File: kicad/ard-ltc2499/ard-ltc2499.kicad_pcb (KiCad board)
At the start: 2 copper layers, 68.6 x 53.3 mm, 8 parts, among them P1 Power, P2 Analog, P3 Digital, P4 Digital, P5 CONN_01X01, P6 CONN_01X01, P7 CONN_01X01, P8 CONN_01X01

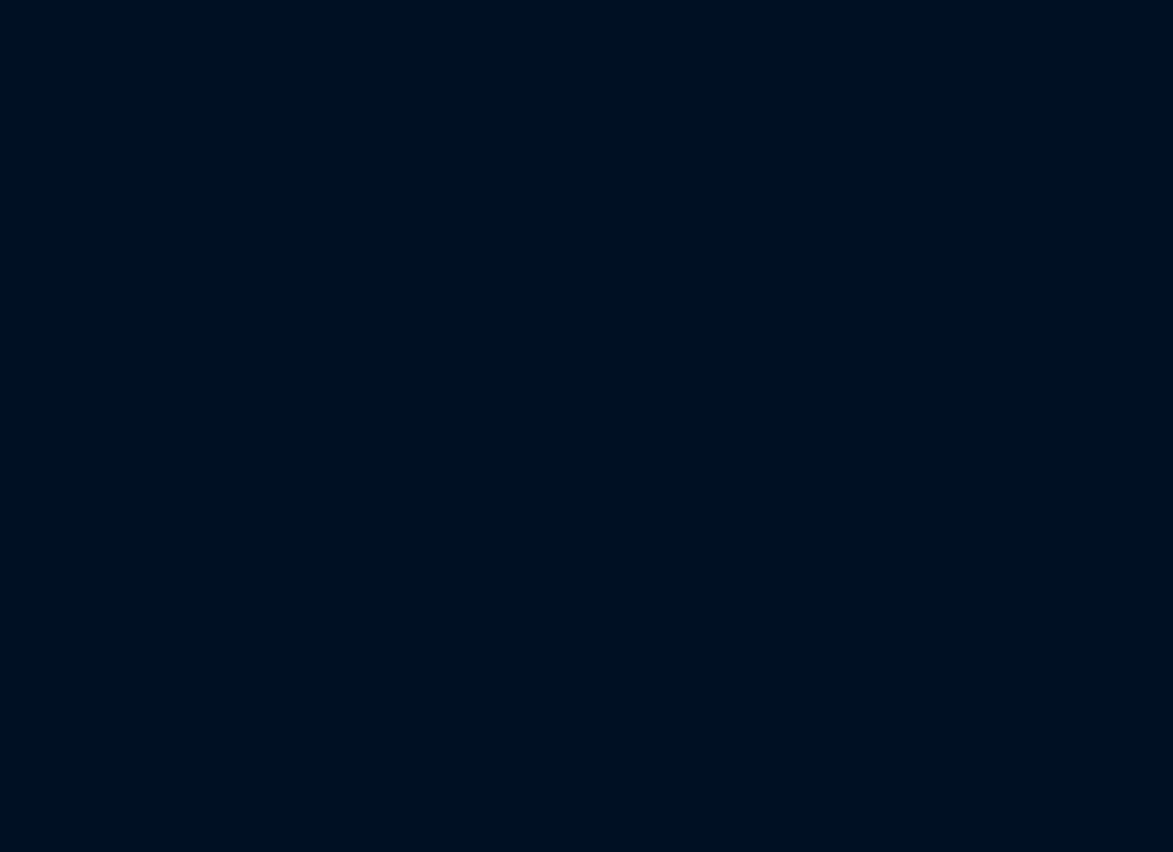
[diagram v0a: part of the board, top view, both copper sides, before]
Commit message: Updated PCB with schematic edits
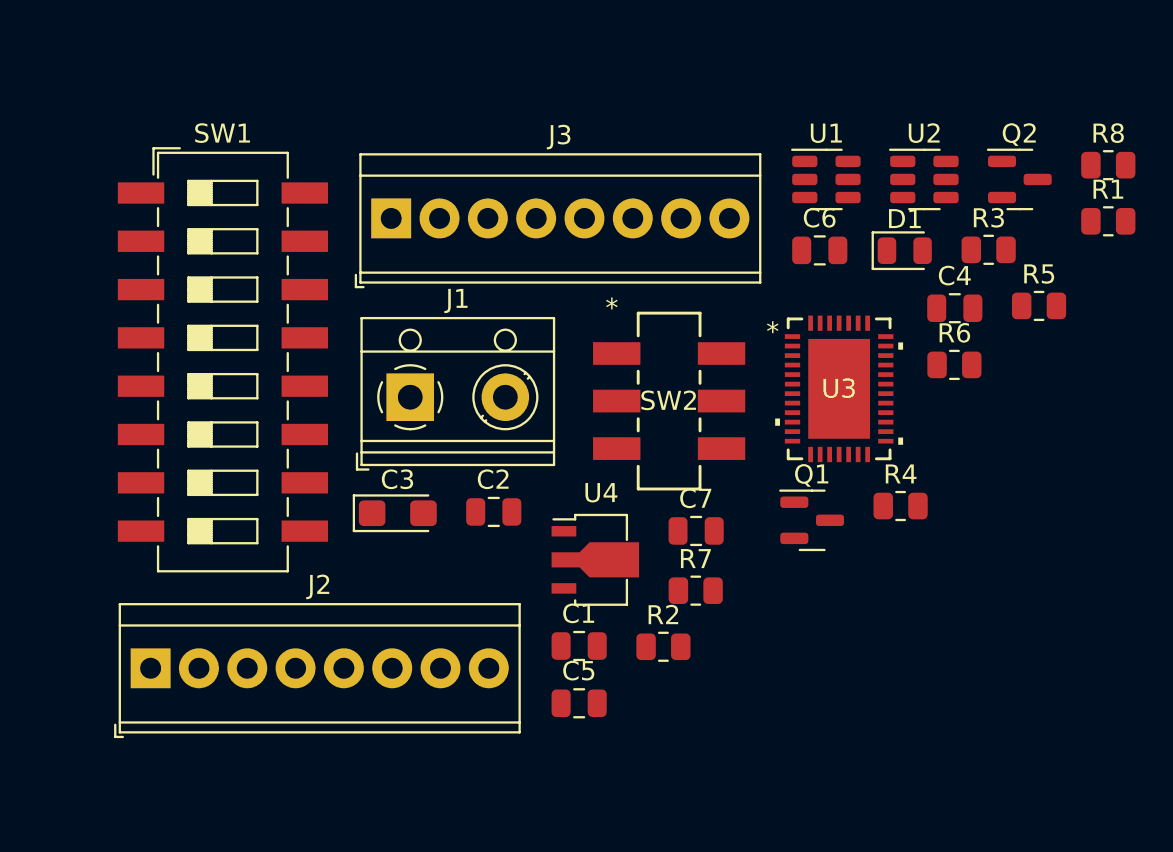
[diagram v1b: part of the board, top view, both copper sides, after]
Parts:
- added C1: 0.1uF, Capacitor_SMD:C_0805_2012Metric, F.Cu at (213.7, 111.5)
- added C2: 1uF, Capacitor_SMD:C_0805_2012Metric, F.Cu at (209.2, 104.4)
- added C3: 22uF, Capacitor_Tantalum_SMD:CP_EIA-3216-18_Kemet-A, F.Cu at (204.1, 104.5)
- added C4: 0.1uF, Capacitor_SMD:C_0805_2012Metric, F.Cu at (233.4, 93.7)
- added C5: 10uF, Capacitor_SMD:C_0805_2012Metric, F.Cu at (213.7, 114.5)
- added C6: 10uF, Capacitor_SMD:C_0805_2012Metric, F.Cu at (226.3, 90.7)
- added C7: 2.2uF, Capacitor_SMD:C_0805_2012Metric, F.Cu at (219.8, 105.4)
- added D1: GREEN LED, LED_SMD:LED_0805_2012Metric, F.Cu at (230.8, 90.7)
- added J1: Screw_Terminal_01x02, TerminalBlock_RND:TerminalBlock_RND_205-00012_1x02_P5.00mm_Horizontal, F.Cu at (204.8, 98.4)
- added J2: Screw_Terminal_01x08, TerminalBlock_TE-Connectivity:TerminalBlock_TE_282834-8_1x08_P2.54mm_Horizontal, F.Cu at (191.1, 112.7)
- added J3: Screw_Terminal_01x08, TerminalBlock_TE-Connectivity:TerminalBlock_TE_282834-8_1x08_P2.54mm_Horizontal, F.Cu at (203.8, 89.0)
- added Q1: BSS138, Package_TO_SOT_SMD:SOT-23, F.Cu at (225.9, 104.9)
- added Q2: BSS138, Package_TO_SOT_SMD:SOT-23, F.Cu at (236.8, 87.0)
- added R1: 10k, Resistor_SMD:R_0805_2012Metric, F.Cu at (241.5, 89.2)
- added R2: 10k, Resistor_SMD:R_0805_2012Metric, F.Cu at (218.1, 111.5)
- added R3: 1k, Resistor_SMD:R_0805_2012Metric, F.Cu at (235.2, 90.7)
- added R4: 10k, Resistor_SMD:R_0805_2012Metric, F.Cu at (230.6, 104.1)
- added R5: 10k, Resistor_SMD:R_0805_2012Metric, F.Cu at (237.8, 93.6)
- added R6: 10k, Resistor_SMD:R_0805_2012Metric, F.Cu at (233.4, 96.7)
- added R7: 10k, Resistor_SMD:R_0805_2012Metric, F.Cu at (219.8, 108.6)
- added R8: 1k, Resistor_SMD:R_0805_2012Metric, F.Cu at (241.5, 86.2)
- added SW1: SW_DIP_x08, Button_Switch_SMD:SW_DIP_SPSTx08_Slide_6.7x21.88mm_W8.61mm_P2.54mm_LowProfile, F.Cu at (194.9, 96.6)
- added SW2: SW_Push_DPDT, ISE_UltraLibrarian:SW_JS202011SCQN, F.Cu at (218.4, 98.6)
- added U1: LT6654xxS6, Package_TO_SOT_SMD:TSOT-23-6, F.Cu at (226.7, 87.0)
- added U2: 24AA025E64, Package_TO_SOT_SMD:TSOT-23-6, F.Cu at (231.8, 87.0)
- added U3: LTC2499CUHF-PBF, ISE_UltraLibrarian:QFN-38_UHF_LIT, F.Cu at (227.3, 98.0)
- added U4: AP7381-50Y, ISE_Generic:SOT-89-3, F.Cu at (214.5, 107.0)
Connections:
- net /10(**/SS) renamed /10(**/SS)
- net /11(**/MOSI) renamed /11(**/MOSI)
- P1 pad 1: Net-(P1-Pad1) -> unconnected-(P1-Pad1)
- P2 pad 5: /A4(SDA) -> /A4
- P2 pad 6: /A5(SCL) -> /A5
- P3 pad 1: /A5(SCL) -> /SCL
- P3 pad 2: /A4(SDA) -> /SDA
- P5 pad 1: Net-(P5-Pad1) -> unconnected-(P5-Pad1)
- P6 pad 1: Net-(P6-Pad1) -> unconnected-(P6-Pad1)
- P7 pad 1: Net-(P7-Pad1) -> unconnected-(P7-Pad1)
- P8 pad 1: Net-(P8-Pad1) -> unconnected-(P8-Pad1)

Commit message: Initial placement
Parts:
- added R10: 1k, Resistor_SMD:R_0805_2012Metric, F.Cu at (195.2, 119.5)
- added R9: 1k, Resistor_SMD:R_0805_2012Metric, F.Cu at (195.2, 122.5)
- added TP1: TestPoint, TestPoint:TestPoint_Pad_D1.5mm, B.Cu at (150.2, 60.8)
- added TP10: TestPoint, TestPoint:TestPoint_Pad_D1.5mm, B.Cu at (132.1, 66.9)
- added TP11: TestPoint, TestPoint:TestPoint_Pad_D1.5mm, B.Cu at (142.5, 130.8)
- added TP12: TestPoint, TestPoint:TestPoint_Pad_D1.5mm, F.Cu at (112.1, 104.5)
- added TP13: TestPoint, TestPoint:TestPoint_Pad_D1.5mm, B.Cu at (134.6, 66.0)
- added TP14: TestPoint, TestPoint:TestPoint_Pad_D1.5mm, B.Cu at (145.0, 129.9)
- added TP15: TestPoint, TestPoint:TestPoint_Pad_D1.5mm, B.Cu at (137.2, 66.9)
- added TP16: TestPoint, TestPoint:TestPoint_Pad_D1.5mm, B.Cu at (147.6, 130.8)
- added TP17: TestPoint, TestPoint:TestPoint_Pad_D1.5mm, B.Cu at (139.7, 66.0)
- added TP18: TestPoint, TestPoint:TestPoint_Pad_D1.5mm, B.Cu at (150.1, 129.9)
- added TP2: TestPoint, TestPoint:TestPoint_Pad_D1.5mm, B.Cu at (121.9, 66.9)
- added TP3: TestPoint, TestPoint:TestPoint_Pad_D1.5mm, B.Cu at (132.3, 130.8)
- added TP4: TestPoint, TestPoint:TestPoint_Pad_D1.5mm, B.Cu at (124.5, 66.0)
- added TP5: TestPoint, TestPoint:TestPoint_Pad_D1.5mm, B.Cu at (134.9, 129.9)
- added TP6: TestPoint, TestPoint:TestPoint_Pad_D1.5mm, B.Cu at (127.0, 66.9)
- added TP7: TestPoint, TestPoint:TestPoint_Pad_D1.5mm, B.Cu at (137.4, 130.8)
- added TP8: TestPoint, TestPoint:TestPoint_Pad_D1.5mm, B.Cu at (129.5, 66.0)
- added TP9: TestPoint, TestPoint:TestPoint_Pad_D1.5mm, B.Cu at (140.0, 129.9)
- SW2: value SW_Push_DPDT -> JS202011SCQN
- moved C6 99.4 mm to (128.5, 108.6), turned to 90 degrees
- moved R8 88.9 mm to (161.3, 124.5)
- moved C7 86.5 mm to (133.3, 106.8), turned to 180 degrees
- moved C5 85.8 mm to (128.5, 103.5), turned to -90 degrees
- moved SW2 84.9 mm to (133.5, 97.8), turned to 90 degrees
- moved C4 83.4 mm to (150.4, 101.3)
- moved U1 82.5 mm to (145.0, 92.1), turned to -90 degrees
- moved U3 82.0 mm to (132.6, 111.4), turned to -90 degrees
- moved D1 81.5 mm to (156.6, 124.5)
- moved R1 81.1 mm to (160.7, 95.9)
- moved J3 80.9 mm to (132.3, 126.9)
- moved R5 79.4 mm to (160.2, 77.4)
- moved R6 79.4 mm to (155.7, 80.5)
- moved U2 78.3 mm to (150.4, 104.6), turned to 180 degrees
- moved R4 73.0 mm to (161.2, 81.4)
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- renumbered U3 to U1, U1 to U2, U4 to U3, U2 to U4
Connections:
- SW1 pad 4: Net-(R3-Pad1) -> Net-(R10-Pad1)
- SW1 pad 6: Net-(R3-Pad1) -> Net-(R9-Pad1)
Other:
- board size 68.6 x 53.3 mm -> 53.3 x 68.6 mm
- board text added: "*"
- board text added: "0 1 2 3 4 5 6 7"
- board text added: "10 11 12 13 14 15"
- board text added: "8 9"
- board text added: "A0 A1 A2 A3 A4 A5"
- board text added: "D7 D6 D5 D4 D3 D2 TX/D1 RX/D0"
- board text added: "N/C IOREF RST 3.3V 5V GND GND VIN"
- board text added: "SCL SDA AREF GND D13 D12 D11 D10 D9 D8"
- board text removed: "1"

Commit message: Complete PCB
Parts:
- TP12: moved to B.Cu
- moved R3 44.8 mm to (163.4, 95.5)
- moved R9 43.5 mm to (163.4, 92.7)
- moved R10 43.4 mm to (163.4, 89.9)
- moved SW1 32.0 mm to (160.1, 112.0)
- moved R8 29.8 mm to (132.6, 116.6)
- moved TP12 24.9 mm to (136.4, 109.7), turned to 180 degrees
- moved D1 24.5 mm to (132.6, 119.4), turned to 180 degrees
- moved R7 17.0 mm to (165.9, 69.1), turned to 90 degrees
- moved C1 13.9 mm to (163.6, 78.0)
- moved R1 13.9 mm to (160.0, 82.0)
- moved R2 13.9 mm to (160.0, 84.8)
- moved U4 13.9 mm to (160.0, 78.0)
- moved R4 12.2 mm to (169.7, 72.6), turned to 180 degrees
- moved R6 11.6 mm to (157.6, 69.1), turned to 90 degrees
- moved Q1 8.85 mm to (169.7, 69.1)
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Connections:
- P3 pad 4: GND -> unconnected-(P3-Pad4)
- R1 pad 1: /A0 -> /AD0
- R2 pad 1: /A1 -> /AD1
- SW1 pad 1: GND -> /CA2
- SW1 pad 10: /CA0 -> GND
- SW1 pad 11: /CA1 -> GND
- SW1 pad 12: /CA1 -> Net-(R10-Pad1)
- SW1 pad 13: /CA2 -> GND
- SW1 pad 14: /CA2 -> Net-(R9-Pad1)
- SW1 pad 15: /A0 -> GND
- SW1 pad 16: /A1 -> Net-(R3-Pad1)
- SW1 pad 2: GND -> /CA2
- SW1 pad 3: GND -> /CA1
- SW1 pad 4: Net-(R10-Pad1) -> /CA1
- SW1 pad 5: GND -> /CA0
- SW1 pad 6: Net-(R9-Pad1) -> /CA0
- SW1 pad 7: GND -> /AD1
- SW1 pad 8: Net-(R3-Pad1) -> /AD0
- SW1 pad 9: /CA0 -> GND
- U4 pad 4: /A1 -> /AD1
- U4 pad 5: /A0 -> /AD0
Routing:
- net GND: track 0.00 -> 112.0 mm, vias 0 -> 22
- net VCC: track 0.00 -> 104.2 mm, vias 0 -> 27
- net /IOREF: track 0.00 -> 80.4 mm
- net /AD0: track 0.00 -> 46.1 mm
- net /VREF: track 0.00 -> 44.1 mm, vias 0 -> 3
- net Net-(J3-Pad1): track 0.00 -> 43.1 mm
- net /AD1: track 0.00 -> 42.7 mm
- net Net-(J3-Pad2): track 0.00 -> 40.5 mm
- net Net-(J3-Pad3): track 0.00 -> 39.7 mm
- net Net-(J3-Pad7): track 0.00 -> 38.5 mm
- net Net-(J3-Pad8): track 0.00 -> 38.4 mm
- net Net-(J3-Pad4): track 0.00 -> 37.5 mm
- net /SCL_5V: track 0.00 -> 37.4 mm
- net Net-(J3-Pad5): track 0.00 -> 36.8 mm
- net Net-(J3-Pad6): track 0.00 -> 36.7 mm
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- added copper zone on F.Cu, net /VREF
- added copper zone on F.Cu, net /Vin
- added copper zone on B.Cu, net GND
- added copper zone on F.Cu, net GND
- added copper zone on B.Cu, net VCC
- added copper zone on F.Cu, net VCC
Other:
- board text added: "4.096V REF COM"
- board text added: "AD0 AD1"
- board text added: "ARD-LTC2499 v2.0 Iowa Scaled Engineering http://www.iascaled.com CC BT-SA ©2024"
- board text added: "CA0 L H"
- board text added: "CA1 L H"
- board text added: "CA2 L H"
- board text added: "EEP ADR"
- board text added: "LTC2499 ADR"
- board text added: "ON OFF"
- board text added: "PWR"

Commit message: Fixed typo
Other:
- board text added: "ARD-LTC2499 v2.0 Iowa Scaled Engineering http://www.iascaled.com CC BY-SA ©2024"
- board text removed: "ARD-LTC2499 v2.0 Iowa Scaled Engineering http://www.iascaled.com CC BT-SA ©2024"
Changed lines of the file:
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@@
     (effects (font (size 1.016 1.016) (thickness 0.1524)) (justify right))
   )
-  (gr_text "ARD-LTC2499 v2.0\nIowa Scaled Engineering\nhttp://www.iascaled.com\nCC BT-SA ©2024" (at 121.158 85.598) (layer "F.SilkS")
+  (gr_text "ARD-LTC2499 v2.0\nIowa Scaled Engineering\nhttp://www.iascaled.com\nCC BY-SA ©2024" (at 121.158 85.598) (layer "F.SilkS")
     (effects (font (size 1.016 1.016) (thickness 0.1524)) (justify left))
   )
